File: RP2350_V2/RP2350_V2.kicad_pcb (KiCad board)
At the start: 4 copper layers, 68.8 x 110.6 mm, 140 parts, among them IC1 DMP1045U-7, IC2 DMP1045U-7, IC3 DMP1045U-7, IC4 DMP1045U-7, J1 Conn_01x04_Pin, J3 USB_C_Receptacle_USB2.0_16P, J4 RF_CONNECTOR_5-1814832-2, J5 Conn_01x08_Socket, J6 Conn_01x02_Pin, J7 Conn_01x04_Pin, SW1 PTS 647 SN50 SMTR2 LFS, SW10 PTS 647 SN50 SMTR2 LFS, SW11 PTS 647 SN50 SMTR2 LFS, SW12 PTS 647 SN50 SMTR2 LFS, SW13 PTS 647 SN50 SMTR2 LFS, SW14 PTS 647 SN50 SMTR2 LFS, SW4 PTS 647 SN50 SMTR2 LFS, SW9 PTS 647 SN50 SMTR2 LFS, U1 RP2350_60QFN, U2 W25Q128JVS, U3 TPS62811QWRWYRQ1, U4 MCP73812T-420I-OT, U5 TLV3012AIDCKR, U6 74HC14, X1 ABM8-272-T3

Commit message: Lots of Updatesgit add --allgit add --all
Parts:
- added IC5: DMP1045U-7, My_Footprints:SOT96P240X110-3N, F.Cu at (131.0, 110.6)
- added IC6: DMP1045U-7, My_Footprints:SOT96P240X110-3N, F.Cu at (160.2, 142.9)
- added J10: S0991-46R, My_Footprints:HARWIN_S0991-46R, F.Cu at (150.3, 82.5)
- added J2: S0991-46R, My_Footprints:HARWIN_S0991-46R, F.Cu at (139.4, 52.5)
- added J8: S0991-46R, My_Footprints:HARWIN_S0991-46R, F.Cu at (141.4, 82.5)
- added J9: S0991-46R, My_Footprints:HARWIN_S0991-46R, F.Cu at (150.3, 52.5)
- added R39: 100k, Resistor_SMD:R_0402_1005Metric, F.Cu at (163.8, 142.9)
- R28: value 86.6 -> 110
- R32: value 75 -> 91
- moved J5 14.0 mm to (149.8, 86.7), turned to 180 degrees
- moved SW10 10.4 mm to (122.5, 131.5)
- moved SW13 10.4 mm to (170.0, 131.5)
- moved SW4 9.58 mm to (171.9, 84.9)
- moved SW9 6.44 mm to (122.5, 121.5)
- moved SW12 6.41 mm to (170.0, 121.5)
- moved SW1 4.97 mm to (120.0, 87.5)
- moved R31 4.64 mm to (131.2, 108.1), turned to 0 degrees
- moved G*** 4.55 mm to (157.5, 126.0)
- moved C23 3.70 mm to (168.9, 92.0)
- moved C24 3.70 mm to (165.1, 92.0)
- moved R18 3.70 mm to (170.0, 90.0)
- moved C21 3.70 mm to (172.7, 91.9)
- moved R16 3.70 mm to (173.7, 91.9)
- moved R20 3.70 mm to (166.1, 90.0)
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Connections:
- D5 pad C: GND -> Net-(IC6-S)
- J5 pad 1: +3V3 -> /DISPLAY_BUSY
- J5 pad 2: GND -> /DISPLAY_RESET
- J5 pad 3: /DISPLAY_BUSY -> /DISPLAY_DC
- J5 pad 4: /DISPLAY_RESET -> /SPI1_CS
- J5 pad 5: /DISPLAY_DC -> /SPI1_CLK
- J5 pad 6: /SPI1_CS -> /SPI1_TX
- J5 pad 7: /SPI1_CLK -> GND
- J5 pad 8: /SPI1_TX -> +3V3
- R31 pad 1: /UVLO_RST -> /RUN
- R31 pad 2: /RUN -> Net-(IC5-S)
- U1 pad 12: SPIO_RX -> unconnected-(U1-GPIO8-Pad12)
- U1 pad 16: uC_RESET -> SPIO_RX
- U1 pad 17: uC_BUSY -> uC_RESET
- U1 pad 18: DIO1 -> unconnected-(U1-GPIO14-Pad18)
- U1 pad 27: unconnected-(U1-GPIO16-Pad27) -> uC_BUSY
- U1 pad 28: unconnected-(U1-GPIO17-Pad28) -> DIO1
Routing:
- net /SWD: track 31.7 -> 45.9 mm
- net VBUS: track 42.5 -> 56.4 mm
- net GND: track 195.4 -> 208.2 mm, vias 366 -> 442
- net Net-(R24-Pad2): track 64.8 -> 75.4 mm
- net DIO1: track 33.2 -> 43.5 mm
- net uC_BUSY: track 34.4 -> 43.7 mm
- net Net-(R18-Pad2): track 53.4 -> 61.3 mm
- net /DISPLAY_BUSY: track 21.0 -> 28.2 mm
- net Net-(R23-Pad2): track 58.0 -> 64.6 mm
- net uC_RESET: track 35.3 -> 40.2 mm
- net /DISPLAY_RESET: track 23.2 -> 27.9 mm
- net Net-(R20-Pad2): track 75.2 -> 70.9 mm
- net Net-(IC6-S): track 0.00 -> 3.86 mm
- net Net-(IC5-S): track 0.00 -> 3.84 mm
- net /BTN_MACRO_C: track 28.1 -> 31.4 mm
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- added copper zone on B.Cu, net GND
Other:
- board size 68.8 x 110.6 mm -> 68.9 x 113.7 mm

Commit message: optimizations, refinements
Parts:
- moved J9 24.0 mm to (130.3, 65.6), turned to 90 degrees
- moved J10 16.9 mm to (150.3, 65.6), turned to 90 degrees
- moved G*** 14.9 mm to (167.1, 57.4)
- moved R39 12.8 mm to (151.1, 144.5)
- moved IC6 5.18 mm to (155.0, 142.9), turned to 180 degrees
- moved G*** 2.10 mm to (155.6, 126.9)
- moved D4 1.79 mm to (155.4, 145.5)
- moved R28 1.79 mm to (152.7, 145.5)
- moved J8 1.63 mm to (142.2, 81.1)
- moved C47 1.44 mm to (146.7, 77.0)
- moved ? 1.44 mm to (146.3, 74.5)
- moved ? 1.44 mm to (145.0, 74.5)
- moved ? 1.44 mm to (145.0, 73.2)
- moved ? 1.44 mm to (146.3, 73.2)
- moved C48 1.44 mm to (139.3, 70.3)
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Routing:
- net VBUS: track 56.4 -> 42.3 mm
- net GND: track 208.2 -> 194.1 mm, vias 442 -> 618
- net /SWD: track 45.9 -> 32.7 mm
- net /SPI1_CLK: track 34.3 -> 28.6 mm
- net /SPI1_TX: track 32.1 -> 28.7 mm
- net /SWCLK: track 35.4 -> 38.2 mm
- net Net-(IC6-S): track 3.86 -> 1.79 mm
- net Net-(IC6-G): track 2.93 -> 5.00 mm
- net SPI0_TX: track 42.1 -> 43.7 mm
- net uC_BUSY: track 43.7 -> 45.3 mm
- net SPIO_RX: track 41.0 -> 42.6 mm
- net SPIO_CLK: track 43.8 -> 45.2 mm
- net uC_RESET: track 40.2 -> 41.6 mm
- net CS/NSS: track 46.2 -> 47.7 mm
- net /SX1262/DIO2: track 25.5 -> 26.8 mm
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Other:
- board size 68.9 x 113.7 mm -> 68.8 x 115.1 mm

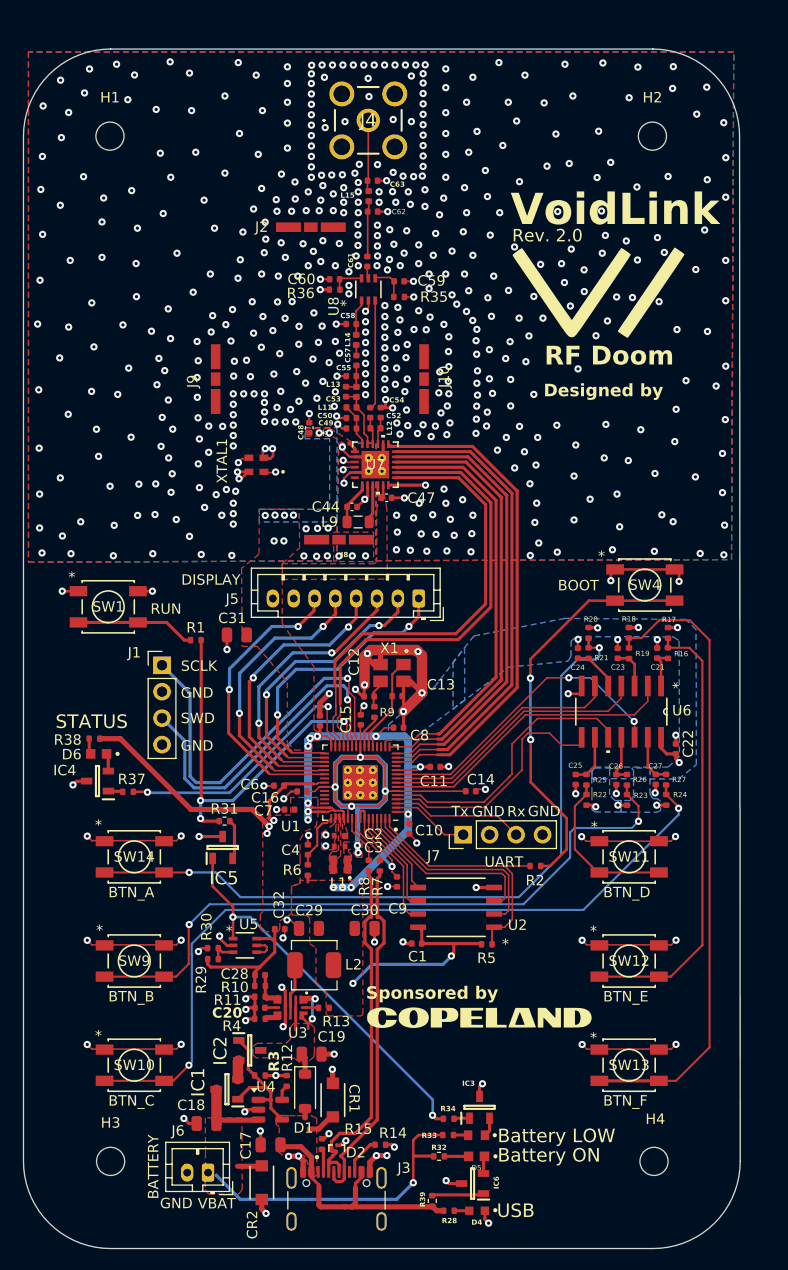
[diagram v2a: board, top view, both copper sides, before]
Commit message: added 3V3 input to ADC, fixed edge cut DRCs
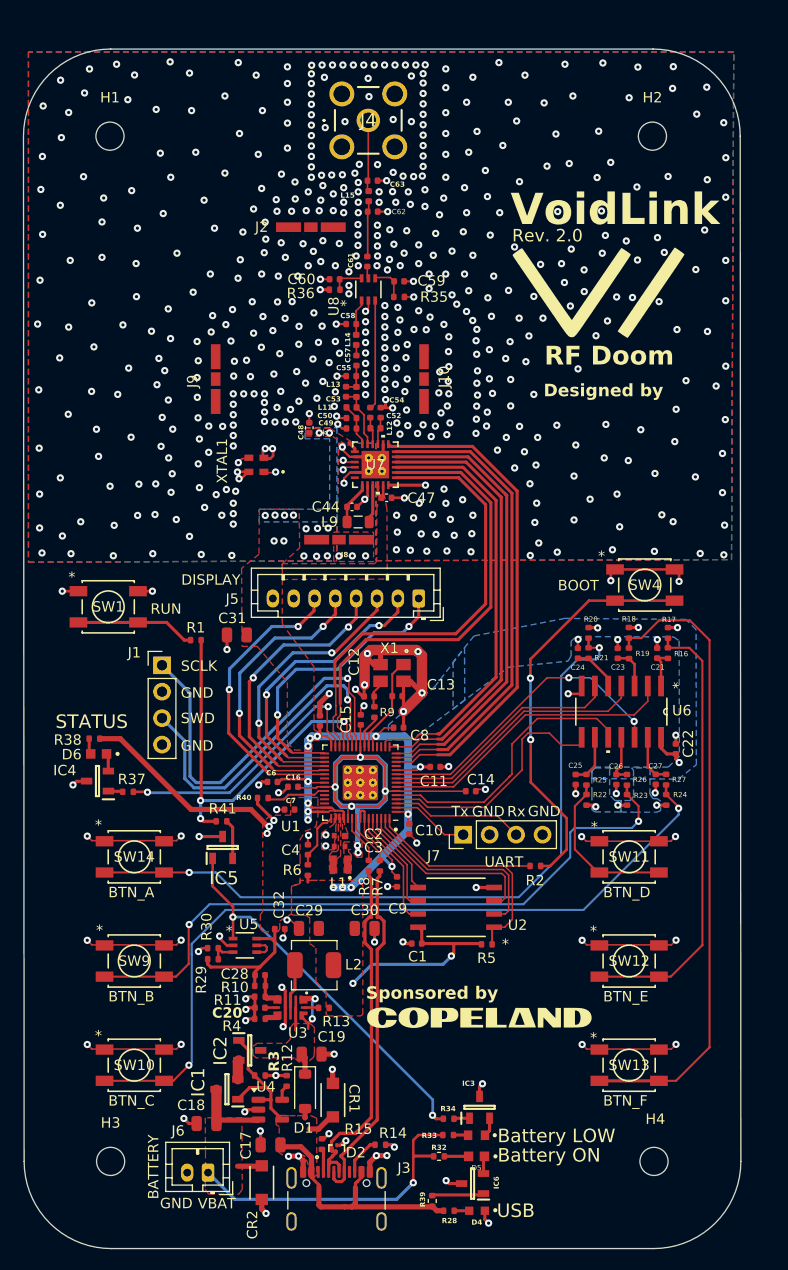
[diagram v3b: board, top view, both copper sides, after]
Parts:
- removed R31: 10k, Resistor_SMD:R_0402_1005Metric
- added R40: 1k, Resistor_SMD:R_0402_1005Metric, F.Cu at (134.8, 105.8)
- added R41: 1k, Resistor_SMD:R_0402_1005Metric, F.Cu at (130.9, 108.1)
- moved C16 0.99 mm to (137.7, 104.8)
- moved C6 0.72 mm to (135.8, 104.3)
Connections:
- U1 pad 40: unconnected-(U1-GPIO26_ADC0-Pad40) -> Net-(U1-GPIO26_ADC0)
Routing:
- net Net-(U1-GPIO26_ADC0): track 0.00 -> 5.81 mm
- net +3V3: track 184.2 -> 182.8 mm, vias 34 -> 35
- net +1V1: track 54.4 -> 55.4 mm
- net /VBAT: track 39.7 -> 40.6 mm
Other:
- board size 68.8 x 115.1 mm -> 68.9 x 115.1 mm

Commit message: DFM progress
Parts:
- moved R1 2.74 mm to (128.3, 88.0)
- moved R2 2.49 mm to (160.3, 114.8)
- moved ? 1.24 mm to (145.0, 72.0)
- moved ? 1.24 mm to (146.3, 72.0)
- moved C44 1.24 mm to (143.4, 76.7)
- moved C47 1.24 mm to (146.7, 75.8)
- moved C49 1.24 mm to (143.3, 69.1)
- moved C50 1.24 mm to (143.3, 68.1)
- moved J10 1.24 mm to (150.3, 64.4)
- moved J9 1.24 mm to (130.3, 64.4)
- moved XTAL1 1.24 mm to (134.2, 72.6)
- moved C57 1.24 mm to (143.8, 62.6)
- moved C58 1.24 mm to (143.3, 59.1)
- moved C59 1.24 mm to (147.9, 55.0)
- moved C60 1.24 mm to (141.7, 54.8)
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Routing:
- net /RUN: track 38.3 -> 41.1 mm
- net /~{USB_BOOT}: track 39.0 -> 41.1 mm
- net Net-(C61-Pad1): track 5.36 -> 3.86 mm
- net Net-(C63-Pad2): track 6.86 -> 8.15 mm
- net SPI0_TX: track 43.7 -> 45.0 mm
- net uC_RESET: track 41.6 -> 42.8 mm
- net DIO1: track 44.6 -> 45.8 mm
- net uC_BUSY: track 45.3 -> 46.6 mm
- net CS/NSS: track 47.7 -> 48.9 mm
- net SPIO_RX: track 42.6 -> 43.8 mm
- net SPIO_CLK: track 45.2 -> 46.4 mm
- net /RUN_IN: track 10.7 -> 9.96 mm
- net /SWCLK: track 38.2 -> 37.6 mm
- net GND: track 193.6 -> 193.5 mm, vias 618 -> 639
- net +3V3: track 182.8 -> 182.7 mm, vias 35 -> 33
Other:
- board size 68.9 x 115.1 mm -> 68.9 x 116.2 mm

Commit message: vias smh my head
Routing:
- net GND: vias 639 -> 638
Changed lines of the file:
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@@
 	)
 	(via
-		(at 165.23 80.234941)
-		(size 0.6)
-		(drill 0.3)
-		(layers "F.Cu" "B.Cu")
-		(free yes)
-		(net 1)
-	)
-	(via
 		(at 138.09 63.6825)
 		(size 0.7)
@@
 	)
 	(via
-		(at 156.75 62.964941)
-		(size 0.6)
-		(drill 0.3)
-		(layers "F.Cu" "B.Cu")
-		(free yes)
-		(net 1)
-	)
-	(via
 		(at 138.94 47.5)
 		(size 0.7)
@@
 	)
 	(via
-		(at 125.23 54.974941)
-		(size 0.6)
-		(drill 0.3)
-		(layers "F.Cu" "B.Cu")
-		(free yes)
-		(net 1)
-	)
-	(via
 		(at 168.767689 105.426765)
 		(size 0.7)
@@
 	)
 	(via
+		(at 157.88 68.36)
+		(size 0.7)
+		(drill 0.3)
+		(layers "F.Cu" "B.Cu")
+		(free yes)
+		(net 1)
+	)
+	(via
 		(at 162.975 41.092441)
 		(size 0.7)
@@
 	)
 	(via
+		(at 129.86 53.81)
+		(size 0.7)
+		(drill 0.3)
+		(layers "F.Cu" "B.Cu")
+		(free yes)
+		(net 1)
+	)
+	(via
 		(at 117.725 37.149882)
 		(size 0.7)
@@
 	)
 	(via
+		(at 163.07 74.68)
+		(size 0.7)
+		(drill 0.3)
+		(layers "F.Cu" "B.Cu")
+		(free yes)
+		(net 1)
+	)
+	(via
 		(at 133.1875 127.2175)
 		(size 0.7)
@@
 	)
 	(via
-		(at 128.64 62.644941)
+		(at 156.83 62.93)
 		(size 0.7)
 		(drill 0.3)
@@
 	)
 	(via
-		(at 117.7 75.184941)
-		(size 0.6)
+		(at 128.64 62.644941)
+		(size 0.7)
 		(drill 0.3)
 		(layers "F.Cu" "B.Cu")
@@
 	)
 	(via
+		(at 127.87 51.06)
+		(size 0.7)
+		(drill 0.3)
+		(layers "F.Cu" "B.Cu")
+		(free yes)
+		(net 1)
+	)
+	(via
 		(at 136.775 119.285)
 		(size 0.7)
@@
 	)
 	(via
-		(at 129.69 53.732441)
-		(size 0.6)
-		(drill 0.3)
-		(layers "F.Cu" "B.Cu")
-		(free yes)
-		(net 1)
-	)
-	(via
 		(at 155 52.5225)
 		(size 0.7)
@@
 	)
 	(via
-		(at 156.84 60.044941)
-		(size 0.6)
+		(at 152.96 53.54)
+		(size 0.7)
 		(drill 0.3)
 		(layers "F.Cu" "B.Cu")
@@
 	)
 	(via
-		(at 167.16 78.354941)
-		(size 0.6)
-		(drill 0.3)
-		(layers "F.Cu" "B.Cu")
-		(free yes)
-		(net 1)
-	)
-	(via
 		(at 132.48 34.234882)
 		(size 0.7)
@@
 	)
 	(via
-		(at 127.63 51.222441)
-		(size 0.6)
-		(drill 0.3)
-		(layers "F.Cu" "B.Cu")
-		(free yes)
-		(net 1)
-	)
-	(via
-		(at 157.83 68.214941)
-		(size 0.6)
-		(drill 0.3)
-		(layers "F.Cu" "B.Cu")
-		(free yes)
-		(net 1)
-	)
-	(via
 		(at 144.1 43.999882)
 		(size 0.7)
@@
 	)
 	(via
-		(at 153 53.68)
-		(size 0.7)
-		(drill 0.3)
-		(layers "F.Cu" "B.Cu")
-		(free yes)
-		(net 1)
-	)
-	(via
 		(at 128.53 64.254941)
 		(size 0.7)
@@
 	)
 	(via
+		(at 117.53 75.04)
+		(size 0.7)
+		(drill 0.3)
+		(layers "F.Cu" "B.Cu")
+		(free yes)
+		(net 1)
+	)
+	(via
 		(at 134.44028 104.60028)
 		(size 0.7)
@@
 	)
 	(via
-		(at 162.94 74.764941)
-		(size 0.6)
-		(drill 0.3)
-		(layers "F.Cu" "B.Cu")
-		(free yes)
-		(net 1)
-	)
-	(via
 		(at 148.58 62.344941)
 		(size 0.7)
@@
 	)
 	(via
+		(at 176.25 76.46)
+		(size 0.7)
+		(drill 0.3)
+		(layers "F.Cu" "B.Cu")
+		(free yes)
+		(net 1)
+	)
+	(via
 		(at 177.5 46.822441)
 		(size 0.7)
@@
 	)
 	(via
+		(at 125.37 55.2)
+		(size 0.7)
+		(drill 0.3)
+		(layers "F.Cu" "B.Cu")
+		(free yes)
+		(net 1)
+	)
+	(via
 		(at 137.1575 117.5575)
 		(size 0.7)
@@
 	)
 	(via
-		(at 176.45 76.464941)
-		(size 0.6)
-		(drill 0.3)
-		(layers "F.Cu" "B.Cu")
-		(free yes)
-		(net 1)
-	)
-	(via
 		(at 113.635 82.01)
 		(size 0.7)
@@
 	)
 	(via
-		(at 132.11 62.694941)
+		(at 156.88 60.08)
 		(size 0.7)
 		(drill 0.3)
@@
 	)
 	(via
-		(at 138.3 66.5325)
+		(at 132.11 62.694941)
 		(size 0.7)
 		(drill 0.3)
@@
 	)
 	(via
-		(at 134.99 66.6525)
+		(at 138.3 66.5325)
 		(size 0.7)
 		(drill 0.3)
@@
 	)
 	(via
-		(at 166.925 45.267441)
+		(at 134.99 66.6525)
 		(size 0.7)
 		(drill 0.3)
@@
 	)
 	(via
-		(at 155.4 40.842441)
+		(at 166.925 45.267441)
 		(size 0.7)
 		(drill 0.3)
@@
 	)
 	(via
-		(at 131.855 82.25)
+		(at 155.4 40.842441)
 		(size 0.7)
 		(drill 0.3)
@@
 	)
 	(via
-		(at 153 53.675)
+		(at 131.855 82.25)
 		(size 0.7)
 		(drill 0.3)
@@
 	)
 	(via
+		(at 167.21 78.42)
+		(size 0.7)
+		(drill 0.3)
+		(layers "F.Cu" "B.Cu")
+		(free yes)
+		(net 1)
+	)
+	(via
 		(at 166.25 75.934941)
 		(size 0.7)
@@
 	)
 	(via
+		(at 165.41 80.33)
+		(size 0.7)
+		(drill 0.3)
+		(layers "F.Cu" "B.Cu")
+		(free yes)
+		(net 1)
+	)
+	(via
 		(at 148.525 34.467441)
 		(size 0.7)
@@
 		(polygon
 			(pts
-				(xy 111.649936 31.2525) (xy 111.608853 83.359617) (xy 141.892635 83.225035) (xy 141.91 79.094941)
+				(xy 111.64899 32.4525) (xy 111.608853 83.359617) (xy 141.892635 83.225035) (xy 141.91 79.094941)
 				(xy 134.449842 79.13545) (xy 134.49 76.894941) (xy 142.003455 76.903355) (xy 142.114275 70.581673)
-				(xy 145.71 70.564861) (xy 145.71 83.266516) (xy 180.556018 83.166374) (xy 180.815753 31.2525)
+				(xy 145.71 70.564861) (xy 145.71 83.266516) (xy 180.556018 83.166374) (xy 180.809749 32.4525)
 			)
 		)

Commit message: final push?
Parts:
- moved C31 8.54 mm to (133.8, 81.8)
- moved C14 1.83 mm to (156.1, 103.9), turned to 90 degrees
- moved C47 0.45 mm to (146.8, 76.2)
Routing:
- net +1V1: track 55.4 -> 57.4 mm
- net GND: track 193.5 -> 192.0 mm, vias 638 -> 640
- net +3V3: track 182.7 -> 183.6 mm

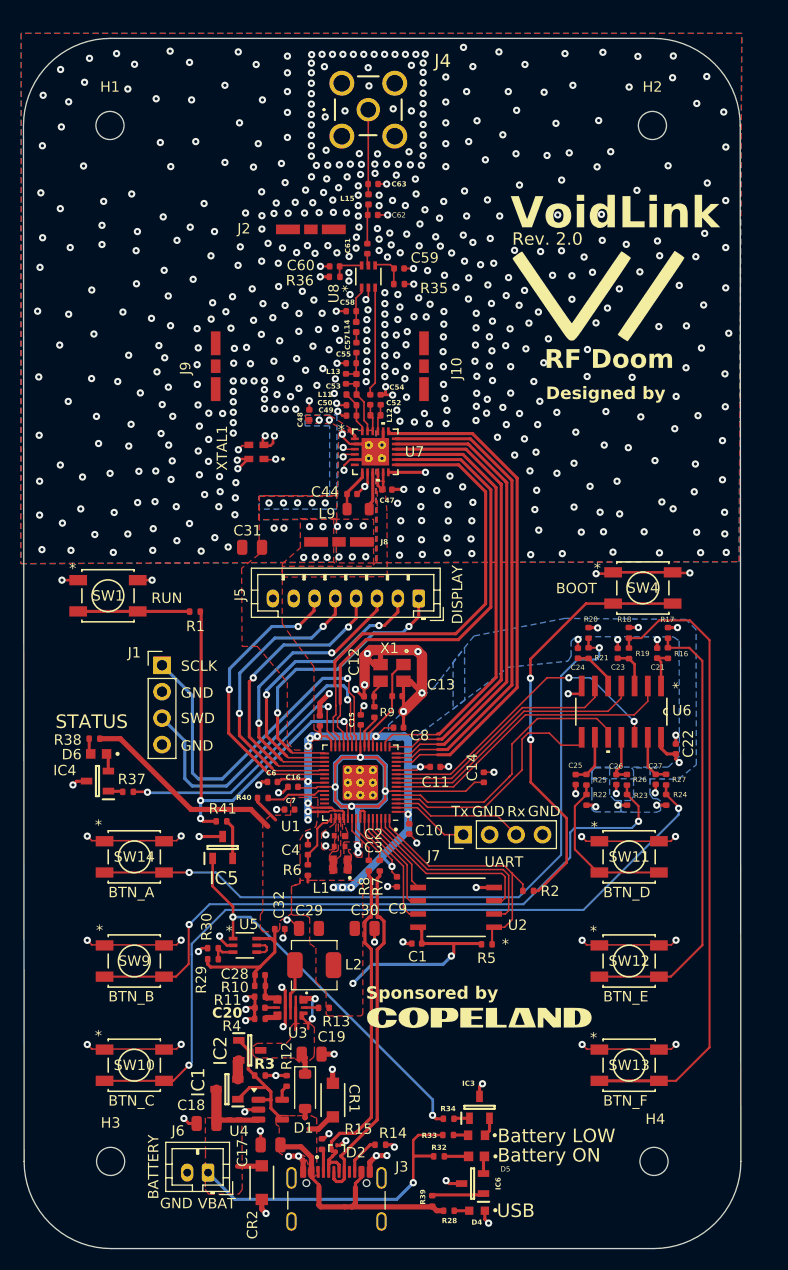
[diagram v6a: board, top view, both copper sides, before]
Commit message: fix display pins on mcu
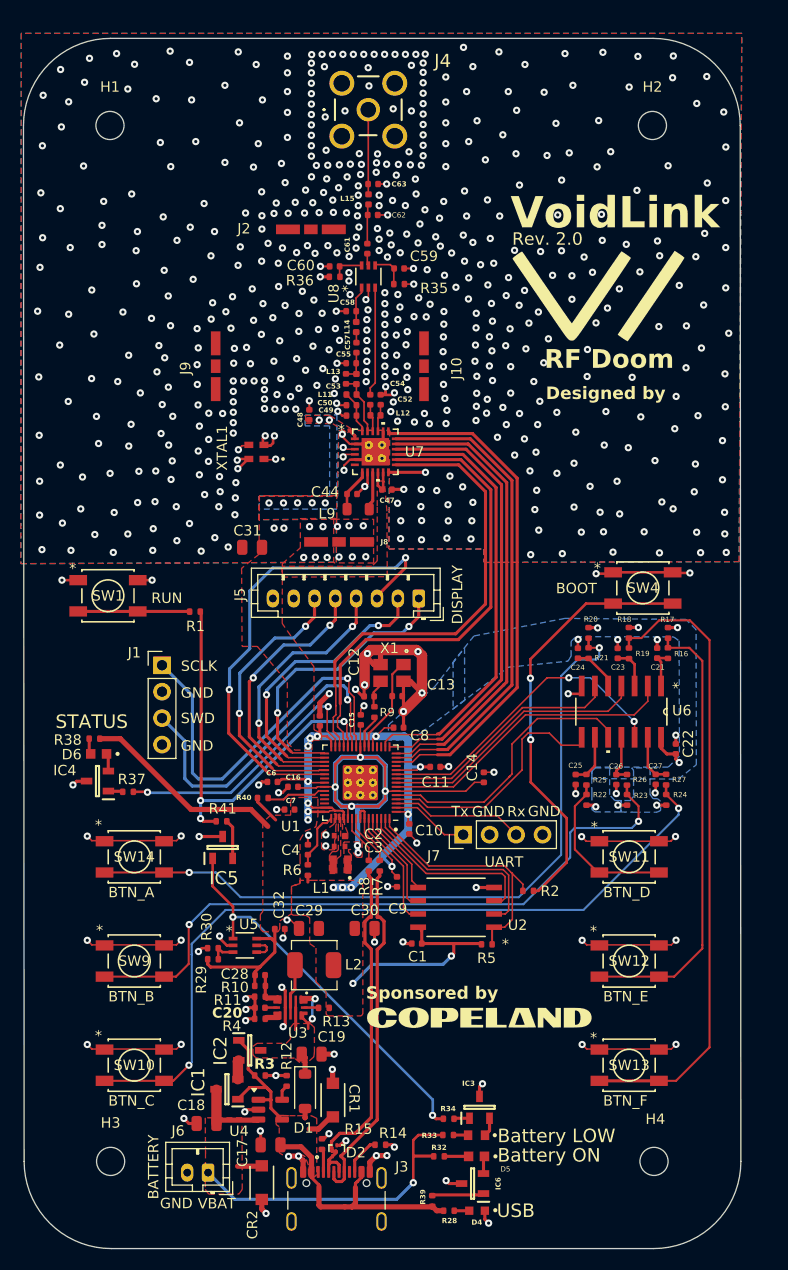
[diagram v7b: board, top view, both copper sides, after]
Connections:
- U1 pad 33: /DISPLAY_DC -> /SPI1_CS
- U1 pad 34: /SPI1_CS -> /SPI1_CLK
- U1 pad 35: /SPI1_CLK -> /SPI1_TX
- U1 pad 36: /SPI1_TX -> /DISPLAY_DC
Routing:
- net /DISPLAY_DC: track 27.6 -> 46.7 mm
- net /SPI1_CS: track 28.5 -> 26.3 mm
- net /SPI1_CLK: track 28.6 -> 26.6 mm
- net /SPI1_TX: track 28.7 -> 26.9 mm
- net GND: track 192.0 -> 192.2 mm, vias 640 -> 637
